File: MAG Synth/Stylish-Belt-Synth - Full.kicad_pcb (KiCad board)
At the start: 2 copper layers, 177.8 x 101.7 mm, 75 parts, among them J0 USB_B, J1 Headphone, J26 WRITE PATCH, J27 PARAM SELECT, J28 PATCH SELECT, J29 MODE, J30 STYLUS, U1 stm32f103c8t6-module-china, U2 XPT8871

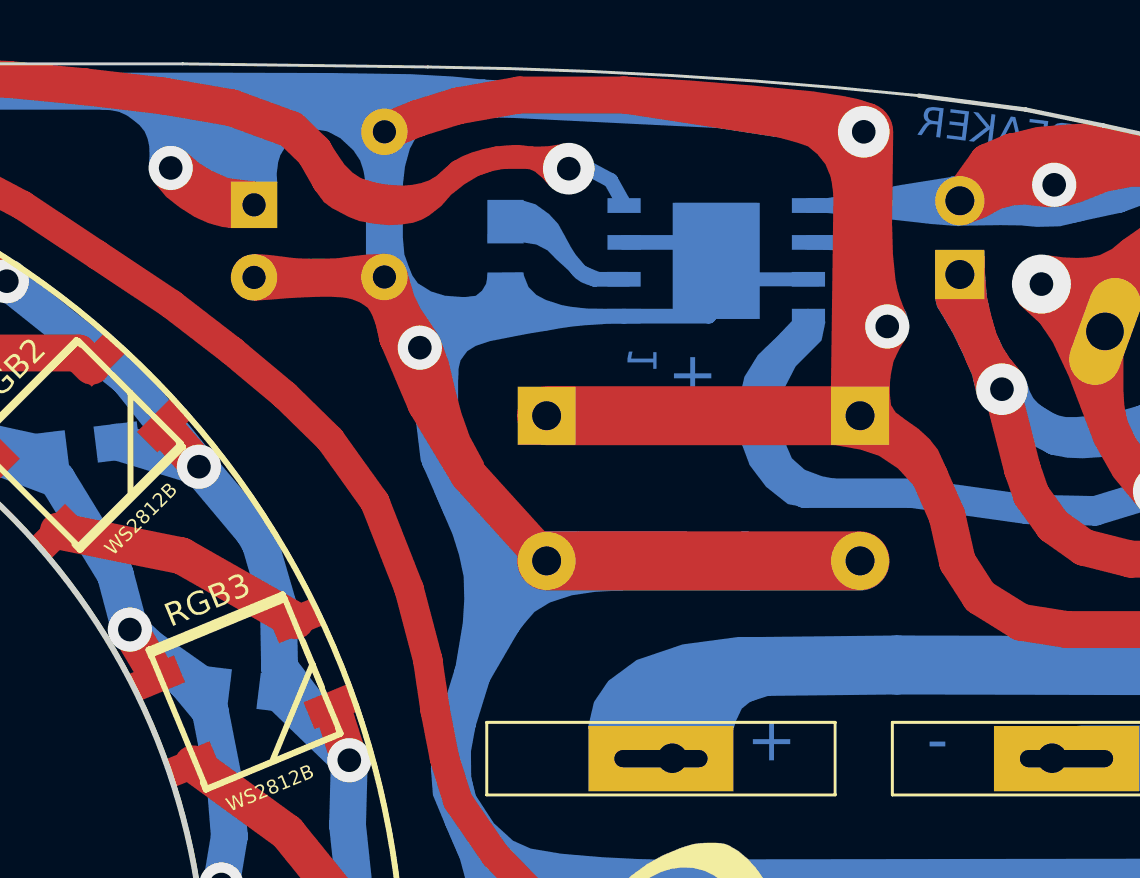
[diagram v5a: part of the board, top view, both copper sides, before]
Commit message: Updated PCB to have heat dissipation for the amplifier chip. Risky last minute changes...
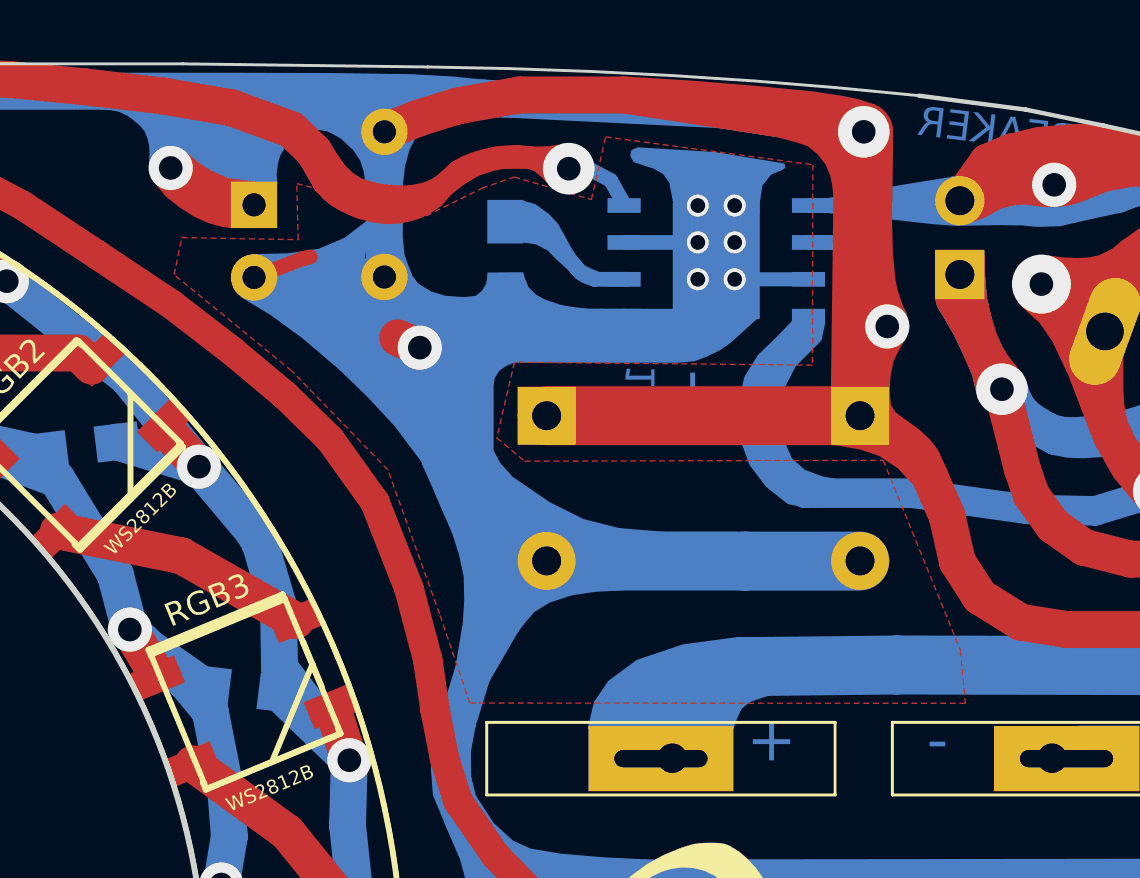
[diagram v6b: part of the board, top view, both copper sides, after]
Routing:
- net GND: track 715.8 -> 691.1 mm, vias 18 -> 24
- added copper zone on F.Cu, net GND

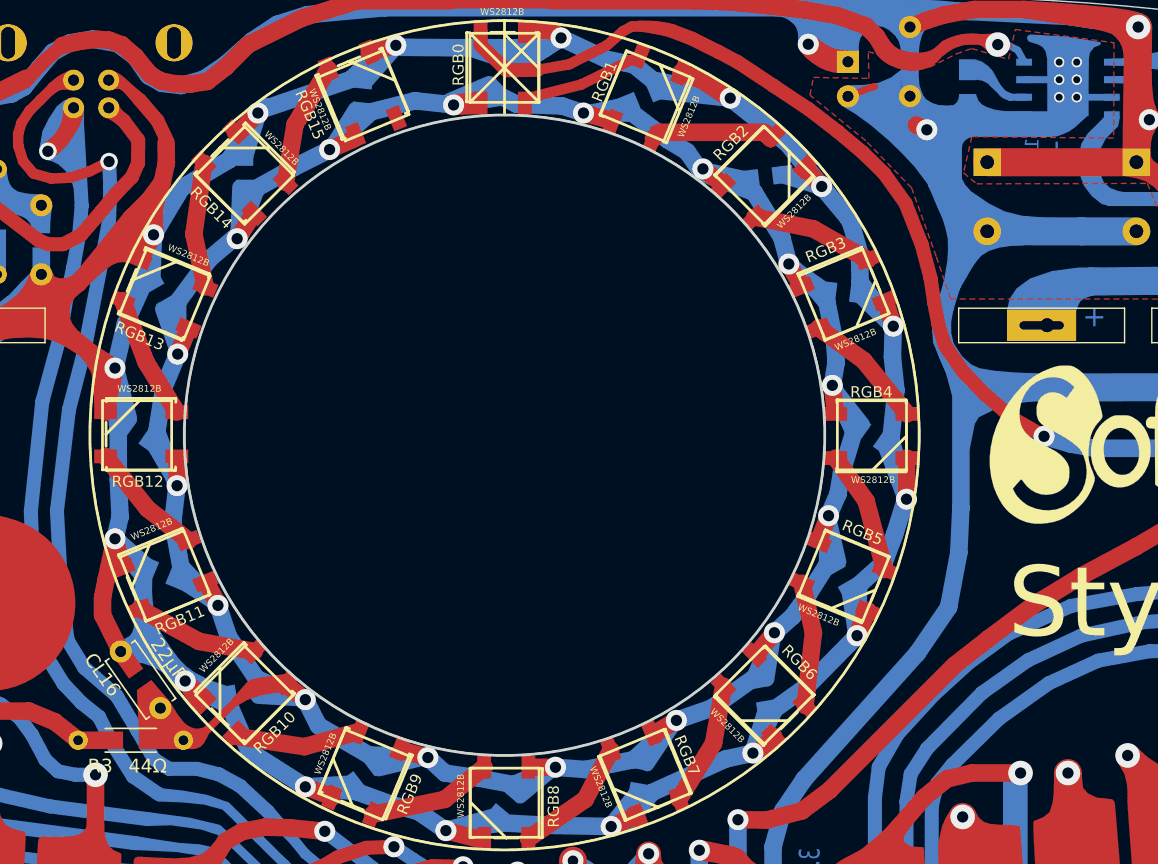
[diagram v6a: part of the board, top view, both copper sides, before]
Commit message: Changed LED ring resistor from 44Ω to 30Ω.
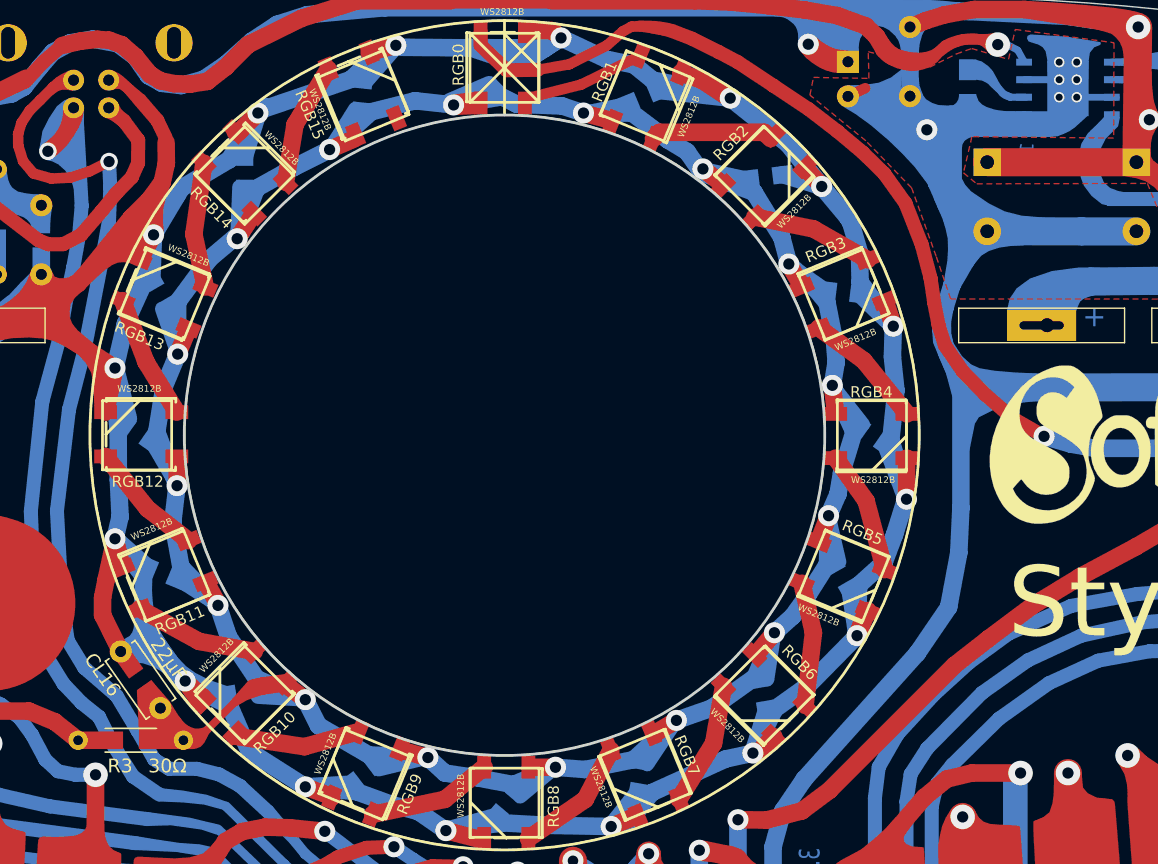
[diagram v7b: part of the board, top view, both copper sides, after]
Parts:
- R3: value 44Ω -> 30Ω
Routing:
- net GND: track 691.1 -> 689.6 mm
